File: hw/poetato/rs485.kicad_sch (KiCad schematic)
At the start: 39 parts, among them J5 61300211121, Q7 FDV304P, Q8 FDV304P, U16 ISO3082, U17 LMR51420XDDCR

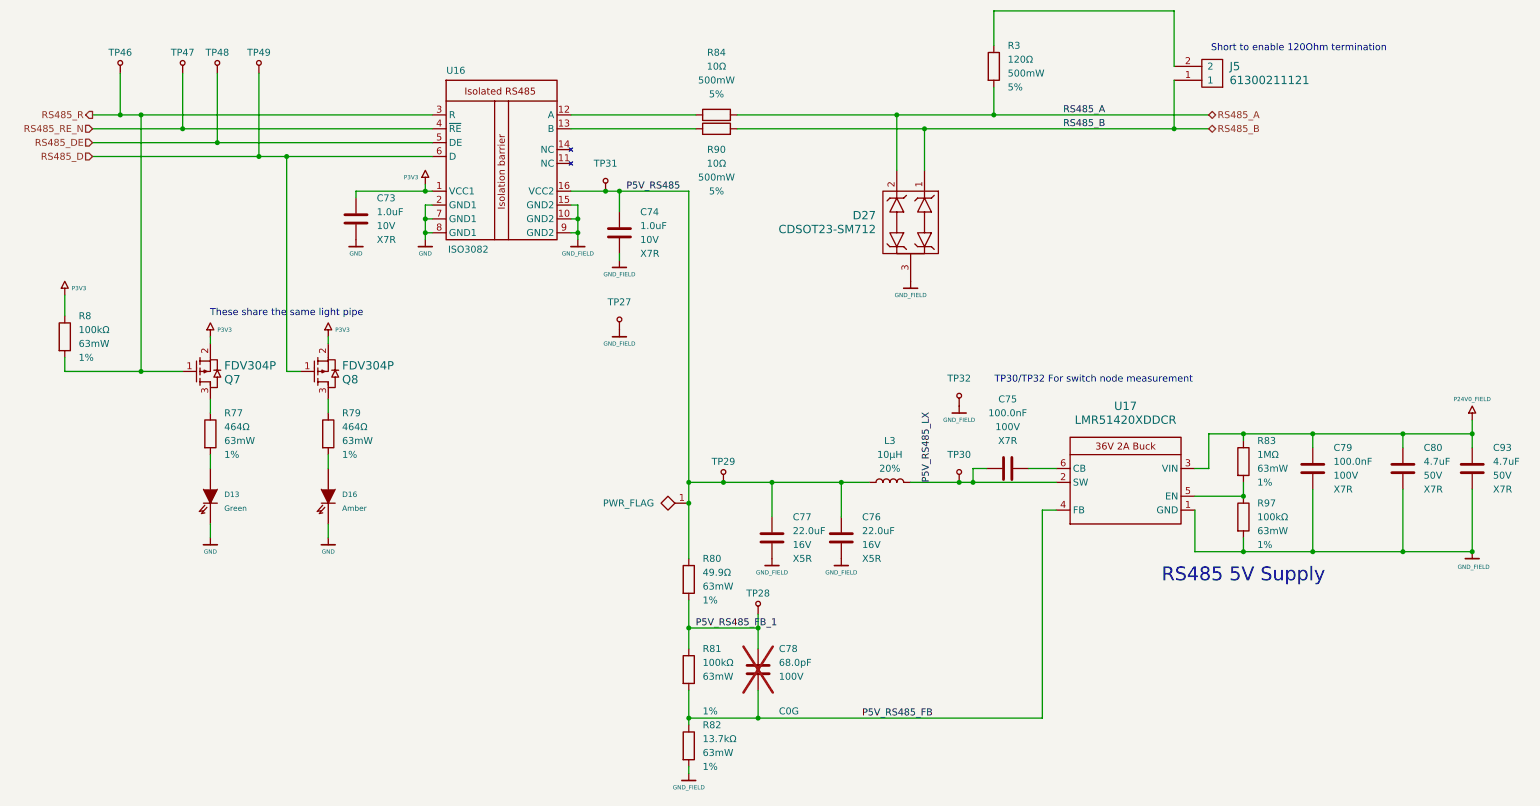
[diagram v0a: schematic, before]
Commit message: hw: sync symbols with kicadlib field text and value updates
Update Symbols from Library for kicadlib 8686346 (field text 1.27 mm) and
5b35b6c (units on misc R/C values). Value text sizes synced to the library
by script, since a Value reset would also reset power-symbol net names.
Restored BOM_Entry Manufacturer/Part Number and the R57 Power field that the
update cleared, and field positions it reset. Nudged R1, C6, Q6 and C75 text
clear of the larger power-symbol labels. ERC clean, netlist unchanged apart
from the intended values.
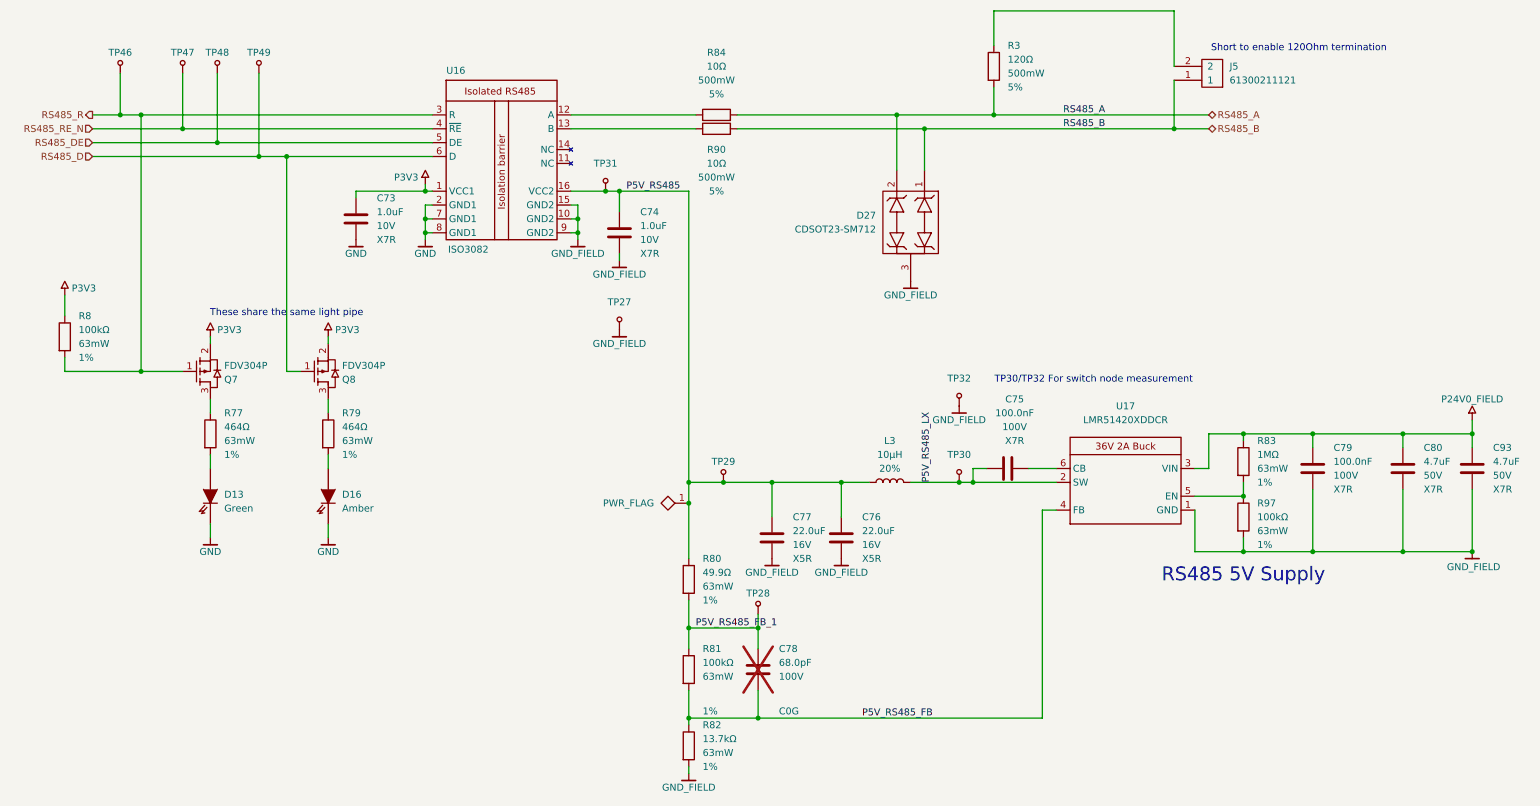
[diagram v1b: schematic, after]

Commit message: hw: move the DC/DC converters to a new top-level Power sheet
power.kicad_sch (page 4) holds the 3.3 V buck (from MCU), the isolated
24 V field supply with its enable FET and LED (from IO) and the RS-485
5 V buck (from RS485). The two bucks are mirrored to read left to right.
The PoE flyback stays on the Ethernet sheet.

P5V_RS485 is now a power symbol and P24V_FIELD_EN goes from MCU to the
Power sheet at the top level. On IO the eFuse moved next to J1, removing
the output loop around the page. The power tree is redrawn more compact
to make room for the new sheet symbol.

Symbols keep their UUIDs and references. ERC clean; every net connects
the same pins as before, 7 nets renamed by the new sheet path.
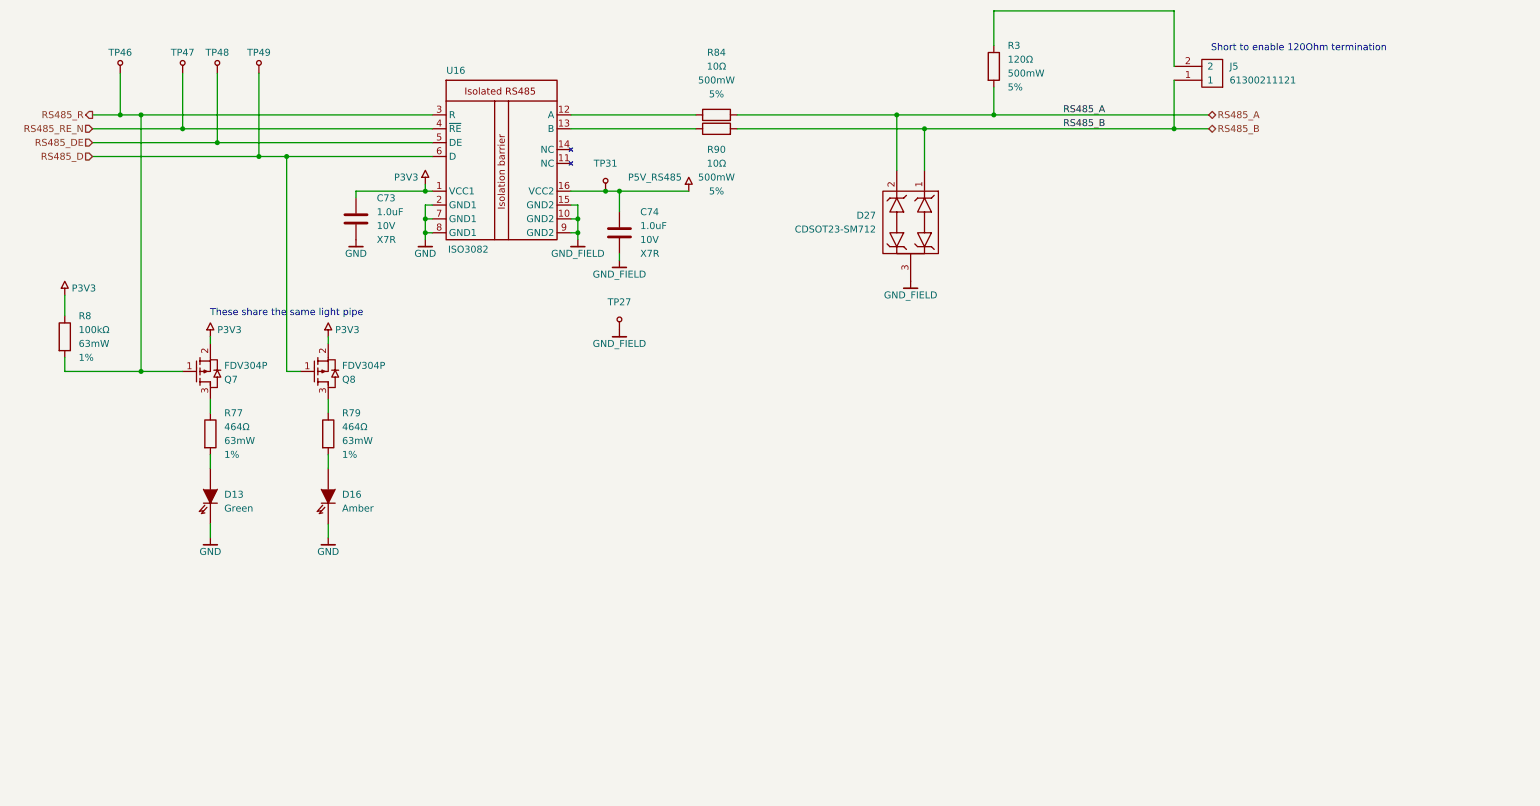
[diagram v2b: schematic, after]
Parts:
- removed C75, C79: ${Capacitance}, Capacitor_SMD:C_0603_1608Metric, symbol cap_mlcc_murata_GRM:GRM/C0603_100n_100V_X7R_10%
- removed C76, C77: ${Capacitance}, Capacitor_SMD:C_0805_2012Metric, symbol cap_mlcc_murata_GRM:GRM/C0805_22u_16V_X5R_20%
- removed C78: ${Capacitance}, Capacitor_SMD:C_0402_1005Metric, symbol cap_mlcc_murata_GRM:GRM/C0402_68p_100V_C0G_5%
- removed C80, C93: ${Capacitance}, Capacitor_SMD:C_1206_3216Metric, symbol cap_mlcc_murata_GRM:GRM/C1206_4u7_50V_X7R_10%
- removed L3: 10µH, Jonas:IHLP2020CZ, symbol ind_power_vishay_ihlp:IHLP/L2020_10u_20_2A5
- removed R80: 49.9Ω, Resistor_SMD:R_0402_1005Metric, symbol res_chip_vishay_crcw:CRCW/R0402_49R9_1_63mW
- removed R81, R97: 100kΩ, Resistor_SMD:R_0402_1005Metric, symbol res_chip_vishay_crcw:CRCW/R0402_100k0_1_63mW
- removed R82: 13.7kΩ, Resistor_SMD:R_0402_1005Metric, symbol res_chip_vishay_crcw:CRCW/R0402_13k7_1_63mW
- removed R83: 1MΩ, Resistor_SMD:R_0402_1005Metric, symbol res_chip_vishay_crcw:CRCW/R0402_1M0_1_63mW
- removed TP28, TP29, TP30, TP32: TP, TestPoint:TestPoint_Pad_D1.0mm, symbol power:TP
- removed U17: LMR51420XDDCR, Package_TO_SOT_SMD:TSOT-23-6, symbol dcdc:LMR51420XDDCR
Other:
- note removed: "RS485 5V Supply"
- note removed: "TP30/TP32 For switch node measurement"
- title: PoEtato - Isolated RS-485 and 5 V supply -> PoEtato - Isolated RS-485
